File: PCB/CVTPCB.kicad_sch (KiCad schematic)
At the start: 18 parts, among them J1 PrimaryPads, J3 SecondaryPads, J4 12V_5V_Regulator, J7 SystemInput, SW1 SW_SPDT, SW2 SW_SPDT

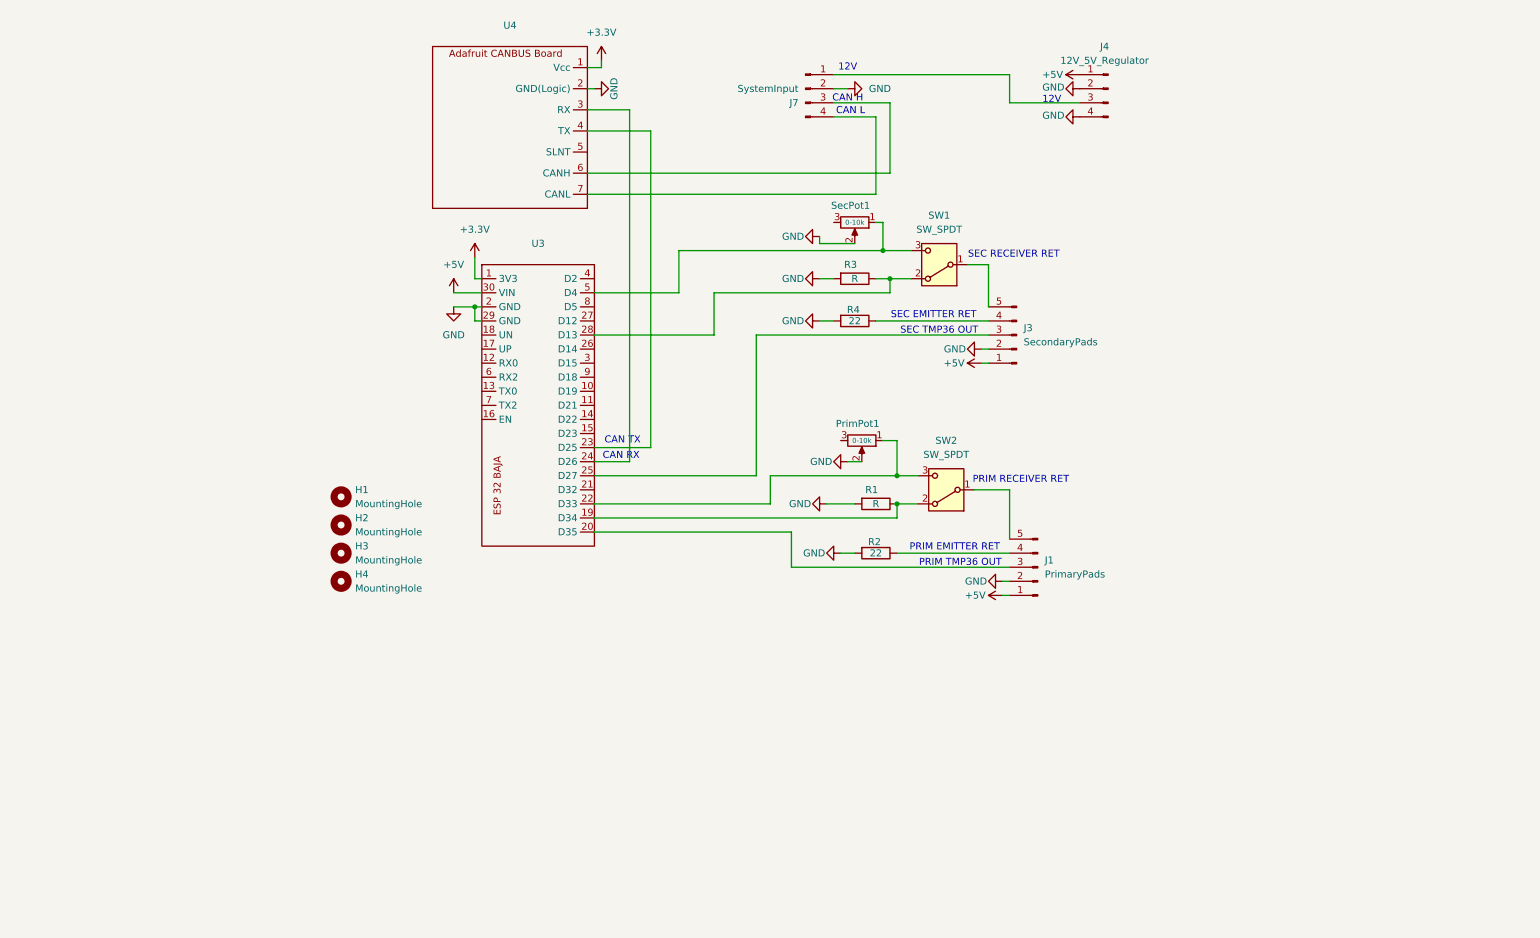
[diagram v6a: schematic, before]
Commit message: Update to new PCB
This PCB features comparators with hysteresis added, surface mount hardware for voltage regulation and CAN protocol, and numerous test points for debugging
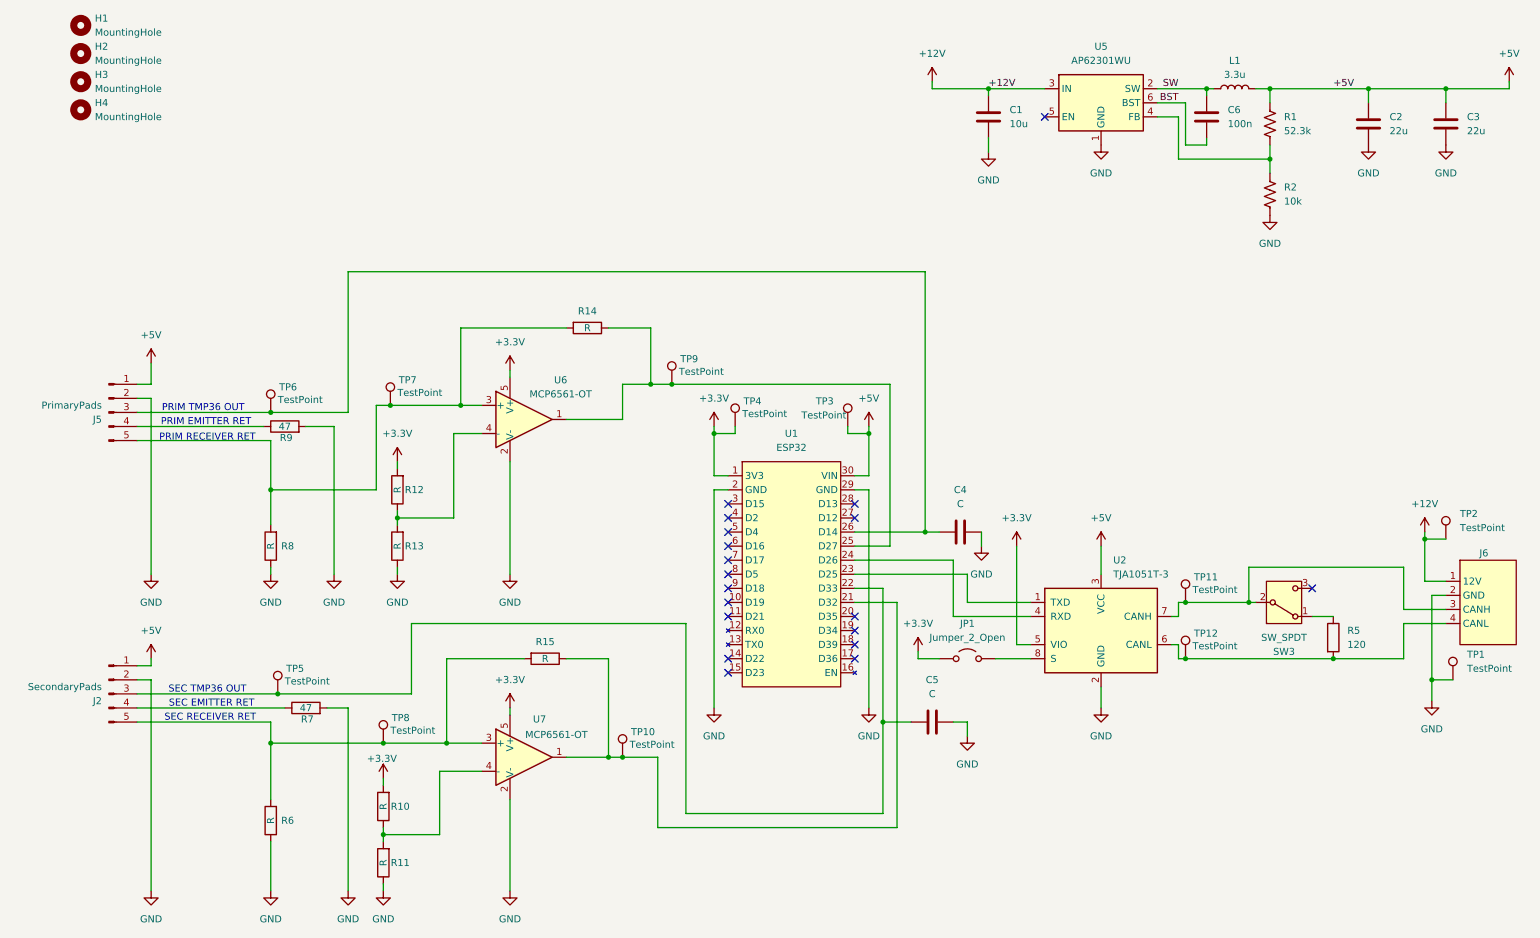
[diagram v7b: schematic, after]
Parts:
- removed J1: PrimaryPads, CVT:Temp_IR_5_Pad_Combo, symbol Connector:Conn_01x05_Pin
- removed J3: SecondaryPads, CVT:Temp_IR_5_Pad_Combo, symbol Connector:Conn_01x05_Pin
- removed J4: 12V_5V_Regulator, CVT:PowerBoard, symbol Connector:Conn_01x04_Pin
- removed J7: SystemInput, CVT:JST4Pin, symbol Connector:Conn_01x04_Pin
- removed PrimPot1, SecPot1: 0-10k, Potentiometer_THT:Potentiometer_Bourns_3339H_Vertical, symbol Device:R_Potentiometer
- removed R1, R3: R, Resistor_THT:R_Axial_DIN0207_L6.3mm_D2.5mm_P10.16mm_Horizontal, symbol Device:R
- removed R2, R4: 22, Resistor_THT:R_Axial_DIN0411_L9.9mm_D3.6mm_P12.70mm_Horizontal, symbol Device:R
- removed SW1, SW2: SW_SPDT, Button_Switch_THT:SW_Slide-03_Wuerth-WS-SLTV_10x2.5x6.4_P2.54mm, symbol Switch:SW_SPDT
- removed U3: ~, CVT:ESP 32 BAJA, symbol ESP 32Pedal:ESP32
- removed U4: ~, CVT:1x7 Connectors, symbol CanBUSPedal:Adafruit_CAN_Pal
- added C1: 10u, Capacitor_SMD:C_0805_2012Metric_Pad1.18x1.45mm_HandSolder, symbol Device:C
- added C2, C3: 22u, Capacitor_SMD:C_0603_1608Metric_Pad1.08x0.95mm_HandSolder, symbol Device:C
- added C4, C5: C, Capacitor_SMD:C_0805_2012Metric_Pad1.18x1.45mm_HandSolder, symbol Device:C
- added C6: 100n, Capacitor_SMD:C_0402_1005Metric_Pad0.74x0.62mm_HandSolder, symbol Device:C
- added J2: SecondaryPads, CVT:Temp_IR_5_Pad_Combo, symbol Connector:Conn_01x05_Pin
- added J5: PrimaryPads, CVT:Temp_IR_5_Pad_Combo, symbol Connector:Conn_01x05_Pin
- added J6: ~, NJIT-Baja-Footprints:Aviation Plug Pads, symbol NJIT-Baja-Symbols:Aviation_Plug_Pads
- added JP1: Jumper_2_Open, Jumper:SolderJumper-2_P1.3mm_Open_Pad1.0x1.5mm, symbol Jumper:Jumper_2_Open
- added L1: 3.3u, Inductor_SMD:L_Taiyo-Yuden_NR-50xx, symbol Device:L
- added R1: 52.3k, Resistor_SMD:R_0402_1005Metric, symbol Device:R_US
- added R10, R11, R12, R13, R14, R15, R6, R8: R, Resistor_THT:R_Axial_DIN0207_L6.3mm_D2.5mm_P10.16mm_Horizontal, symbol Device:R
- added R2: 10k, Resistor_SMD:R_0402_1005Metric, symbol Device:R_US
- added R5: 120, Resistor_SMD:R_1206_3216Metric_Pad1.30x1.75mm_HandSolder, symbol Device:R
- added R7, R9: 47, Resistor_THT:R_Axial_DIN0411_L9.9mm_D3.6mm_P12.70mm_Horizontal, symbol Device:R
- added SW3: SW_SPDT, Button_Switch_SMD:SW_SPDT_CK_JS102011SAQN, symbol Switch:SW_SPDT
- added TP1, TP10, TP11, TP12, TP2, TP3, TP4, TP5, TP6, TP7, TP8, TP9: TestPoint, TestPoint:TestPoint_THTPad_D3.0mm_Drill1.5mm, symbol Connector:TestPoint
- added U1: ESP32, NJIT-Baja-Footprints:ESP32, symbol NJIT-Baja-Symbols:ESP32
- added U2: TJA1051T-3, Package_SO:SOIC-8_3.9x4.9mm_P1.27mm, symbol Interface_CAN_LIN:TJA1051T-3
- added U5: AP62301WU, Package_TO_SOT_SMD:TSOT-23-6, symbol Regulator_Switching:AP62301WU
- added U6, U7: MCP6561-OT, Package_TO_SOT_SMD:SOT-23-5, symbol Comparator:MCP6561-OT
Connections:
- net +3.3V: now also JP1.1 (A), R10.2, R12.2, TP4.1, U1.1 (3V3), U2.5 (VIO), U6.5 (V+), U7.5 (V+)
- net +5V: now also C2.1, C3.1, J2.1 (Pin_1), J5.1 (Pin_1), L1.2, R1.1, TP3.1, U1.30 (VIN), U2.3 (VCC)
- net GND: now also C1.2, C2.2, C3.2, C4.2, C5.2, J2.2 (Pin_2), J5.2 (Pin_2), J6.2 (GND), R11.1, R13.1, R2.2, R6.1, R7.2, R8.1, R9.2, TP1.1, U1.2 (GND), U1.29 (GND), U2.2 (GND), U5.1 (GND), U6.2 (V-), U7.2 (V-)
- new net: R12.1, R13.2, U6.4 (-)
- new net: J5.4 (Pin_4), R9.1
- new net: R14.1, TP9.1, U1.25 (D27), U6.1
- new net: J5.5 (Pin_5), R14.2, R8.2, TP7.1, U6.3 (+)
- new net: R10.1, R11.2, U7.4 (-)
- new net: J2.5 (Pin_5), R15.2, R6.2, TP8.1, U7.3 (+)
- new net: J2.4 (Pin_4), R7.1
- new net: JP1.2 (B), U2.8 (S)
- new net: C4.1, J5.3 (Pin_3), TP6.1, U1.26 (D14)
- new net: R5.1, SW3.1 (A)
- new net: J6.3 (CANH), SW3.2 (B), TP11.1, U2.7 (CANH)
- new net: C5.1, J2.3 (Pin_3), TP5.1, U1.22 (D33)
- new net: R1.2, R2.1, U5.4 (FB)
- new net: R15.1, TP10.1, U1.21 (D32), U7.1
- new net: J6.4 (CANL), R5.2, TP12.1, U2.6 (CANL)
- new net: U1.23 (D25), U2.1 (TXD)
- new net: U1.24 (D26), U2.4 (RXD)
- new net +12V: C1.1, J6.1 (12V), TP2.1, U5.3 (IN)
- new net BST: C6.2, U5.6 (BST)
- new net SW: C6.1, L1.1, U5.2 (SW)
- no-connect marks 0 -> 19
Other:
- note removed: "12V"
- note removed: "CAN H"
- note removed: "CAN L"
- note removed: "CAN RX"
- note removed: "CAN TX"
- moved on the sheet: H1, H2, H3, H4

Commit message: Update PCB to use comparator, includes new GBR and DRL
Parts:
- R10, R11, R12, R13, R14, R15, R6, R8: footprint Resistor_THT:R_Axial_DIN0207_L6.3mm_D2.5mm_P10.16mm_Horizontal -> Resistor_SMD:R_1206_3216Metric_Pad1.30x1.75mm_HandSolder
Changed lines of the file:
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@@
 			)
 		)
-		(property "Footprint" "Resistor_THT:R_Axial_DIN0207_L6.3mm_D2.5mm_P10.16mm_Horizontal"
+		(property "Footprint" "Resistor_SMD:R_1206_3216Metric_Pad1.30x1.75mm_HandSolder"
 			(at 79.248 111.76 90)
 			(effects
@@
 			)
 		)
-		(property "Footprint" "Resistor_THT:R_Axial_DIN0207_L6.3mm_D2.5mm_P10.16mm_Horizontal"
+		(property "Footprint" "Resistor_SMD:R_1206_3216Metric_Pad1.30x1.75mm_HandSolder"
 			(at 76.708 168.91 90)
 			(effects
@@
 			)
 		)
-		(property "Footprint" "Resistor_THT:R_Axial_DIN0207_L6.3mm_D2.5mm_P10.16mm_Horizontal"
+		(property "Footprint" "Resistor_SMD:R_1206_3216Metric_Pad1.30x1.75mm_HandSolder"
 			(at 79.248 101.6 90)
 			(effects
@@
 			)
 		)
-		(property "Footprint" "Resistor_THT:R_Axial_DIN0207_L6.3mm_D2.5mm_P10.16mm_Horizontal"
+		(property "Footprint" "Resistor_SMD:R_1206_3216Metric_Pad1.30x1.75mm_HandSolder"
 			(at 56.388 161.29 90)
 			(effects
@@
 			)
 		)
-		(property "Footprint" "Resistor_THT:R_Axial_DIN0207_L6.3mm_D2.5mm_P10.16mm_Horizontal"
+		(property "Footprint" "Resistor_SMD:R_1206_3216Metric_Pad1.30x1.75mm_HandSolder"
 			(at 104.14 130.302 90)
 			(effects
@@
 			)
 		)
-		(property "Footprint" "Resistor_THT:R_Axial_DIN0207_L6.3mm_D2.5mm_P10.16mm_Horizontal"
+		(property "Footprint" "Resistor_SMD:R_1206_3216Metric_Pad1.30x1.75mm_HandSolder"
 			(at 76.708 158.75 90)
 			(effects
@@
 			)
 		)
-		(property "Footprint" "Resistor_THT:R_Axial_DIN0207_L6.3mm_D2.5mm_P10.16mm_Horizontal"
+		(property "Footprint" "Resistor_SMD:R_1206_3216Metric_Pad1.30x1.75mm_HandSolder"
 			(at 111.76 70.612 90)
 			(effects
@@
 			)
 		)
-		(property "Footprint" "Resistor_THT:R_Axial_DIN0207_L6.3mm_D2.5mm_P10.16mm_Horizontal"
+		(property "Footprint" "Resistor_SMD:R_1206_3216Metric_Pad1.30x1.75mm_HandSolder"
 			(at 56.388 111.76 90)
 			(effects
